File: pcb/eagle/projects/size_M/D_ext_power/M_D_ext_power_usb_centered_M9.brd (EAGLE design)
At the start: 33 parts, among them U1 LM66100DCKR

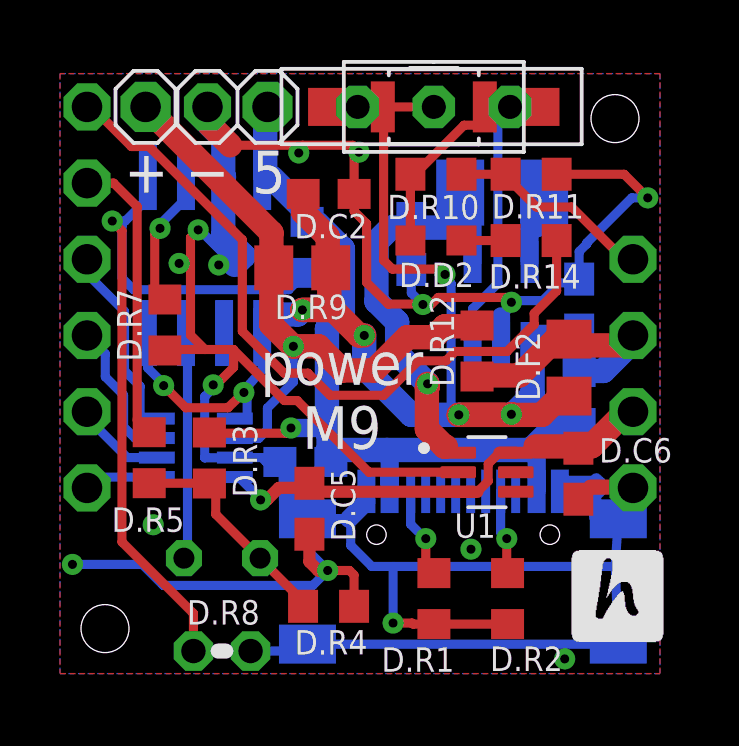
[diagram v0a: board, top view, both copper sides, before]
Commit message: turning on/off is performed by monitoring push button. D flip-flop is not necessary - has problem with button oscilations.
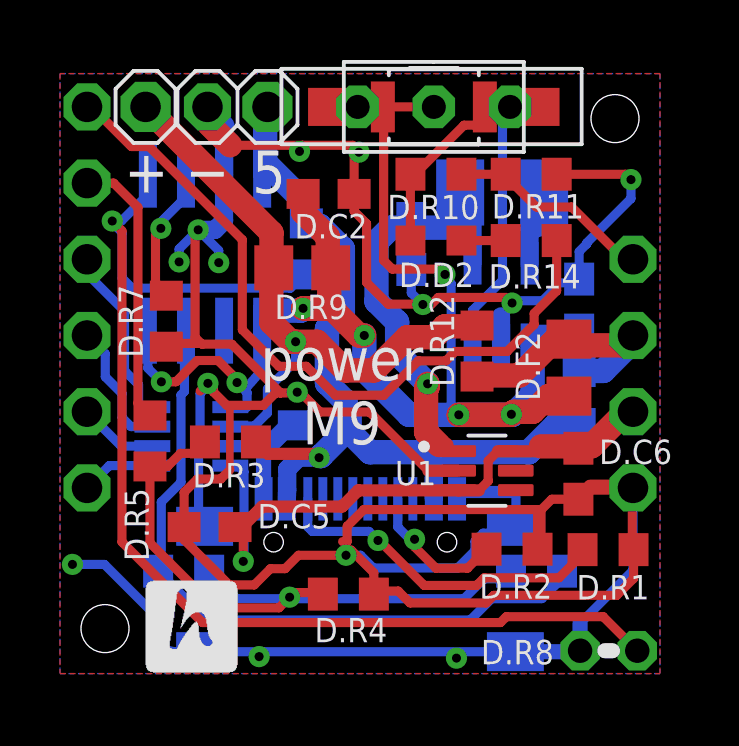
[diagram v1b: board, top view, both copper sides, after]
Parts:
- removed D.D1: LED_1.8, hugo:LED_1.8
- added LED1, LED2: (no value), led:CHIP-LED0603
- D.R10: value 150k -> 100k
- D.R11: value 330k -> 100k
- D.R14: value 680k -> 10k
- moved D.R8 12.9 mm to (18.8, 1.26), turned to 0 degrees
- moved D.R1 6.03 mm to (18.8, 4.63), turned to 0 degrees
- moved U$1 3.44 mm to (10.5, 2.50)
- moved D.C5 3.38 mm to (5.49, 5.38), turned to 0 degrees
- moved D.R2 1.65 mm to (15.6, 4.65), turned to 0 degrees
- moved D.C1 1.31 mm to (9.16, 8.77)
- moved D.R3 0.88 mm to (6.18, 8.22), turned to 0 degrees
- moved D.R4 0.78 mm to (10.1, 3.15)
- moved D.R5 0.56 mm to (3.50, 8.26)
- moved D.U3 0.41 mm to (4.88, 8.41)
- moved D.R7 0.14 mm to (4.05, 12.2)
- moved D.U1 0.08 mm to (5.33, 14.5)
- moved D.R6 0.06 mm to (8.71, 14.7)
- moved D.U2 0.05 mm to (15.2, 12.8)
- moved U1 0.05 mm to (14.7, 7.26)
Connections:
- net CHRG: now also LED1.A1, LED2.A1; no longer D.D1.2
- net N$3: now also LED1.C1, LED2.C1; no longer D.D1.1
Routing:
- net GND: track 123.5 -> 140.1 mm, vias 15 -> 14
- net N$3: track 7.58 -> 23.4 mm
- net CHRG: track 7.79 -> 22.5 mm, vias 0 -> 1
- net N$8: track 26.4 -> 40.4 mm
- net N$4: track 3.06 -> 11.5 mm
- net VCC: track 18.0 -> 22.4 mm
- net N$6: track 2.82 -> 4.88 mm
- net 5V: track 30.0 -> 31.7 mm
- net PA3: track 9.68 -> 9.13 mm

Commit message: power module finalizations (M9)
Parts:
- added D.R15: 0R, rcl:R0603
- moved U1 1.35 mm to (13.6, 6.50)
- moved D.R2 0.46 mm to (15.5, 4.19)
- moved D.U2 0.33 mm to (15.2, 12.5)
- moved D.D2 0.13 mm to (13.0, 15.1)
- moved D.C3 0.10 mm to (17.8, 12.7)
- moved D.R12 0.10 mm to (14.4, 11.4)
- moved D.R13 0.08 mm to (17.8, 9.63)
- moved D.R14 0.08 mm to (16.2, 15.0)
- moved D.F2 0.07 mm to (17.5, 10.7)
- moved D.R4 0.05 mm to (10.1, 3.20)
- moved D.R10 0.05 mm to (13.0, 17.2)
- moved D.R11 0.05 mm to (16.2, 17.2)
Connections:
- net VCC: now also D.R15.1
- net VCC1: now also D.R15.2
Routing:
- net GND: track 140.1 -> 131.9 mm, vias 14 -> 15
- net VCC: track 22.4 -> 23.6 mm
- net IN+: track 52.6 -> 53.3 mm

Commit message: PCB v9
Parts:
- removed D.C5: 100n, rcl:C0603
- removed D.R12, D.R13: 0, rcl:R0603
- removed D.R15: 0R, rcl:R0603
- removed D.R2: 5k1, rcl:R0603
- removed U1: LM66100DCKR, LM66100DCKR:SOT65P210X110-6N
- added Ḋ.C5: 100n, rcl:C0603
- added Ḋ.R12, Ḋ.R13: 0, rcl:R0603
- added Ḋ.R15: 0R, rcl:R0603
- added Ḋ.R2: 5k1, rcl:R0603
- added Ḋ.U3: LM66100DCKR, LM66100DCKR:SOT65P210X110-6N
- renumbered D.C1 to Ḋ.C1, D.C2 to Ḋ.C2, D.C3 to Ḋ.C3, D.C4 to Ḋ.C4, D.C6 to Ḋ.C6, D.D2 to Ḋ.D3, D.F2 to Ḋ.F2, D.J2 to Ḋ.J2, D.J3 to Ḋ.J3, D.L1 to Ḋ.L1, D.LIPOL to Ḋ.LIPOL, D.ON/OFF/RESET to Ḋ.BTN, D.R1 to Ḋ.R1, D.R10 to Ḋ.R10, D.R11 to Ḋ.R11, D.R14 to Ḋ.R14, D.R3 to Ḋ.R3, D.R4 to Ḋ.R4, D.R5 to Ḋ.R5, D.R6 to Ḋ.R6, D.R7 to Ḋ.R7, D.R8 to Ḋ.R8, D.R9 to Ḋ.R9, D.U1 to Ḋ.U1, D.U2 to Ḋ.U2, D.U3 to Ḋ.U4, LED1 to Ḋ.D1, LED2 to Ḋ.D2, U$1 to Ḋ.J1
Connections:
- net 5V: now also Ḋ.R13.1; no longer D.R13.1
- net GND: now also Ḋ.C5.1, Ḋ.R2.2, Ḋ.U3.2; no longer D.C5.1, D.R2.2, U1.2
- net IN-: now also Ḋ.R12.1; no longer D.R12.1
- net N$6: now also Ḋ.R2.1; no longer D.R2.1
- net VCC: now also Ḋ.C5.2, Ḋ.R15.1, Ḋ.U3.3, Ḋ.U3.6; no longer D.C5.2, D.R15.1, U1.3, U1.6
- net VCC1: now also Ḋ.R15.2, Ḋ.U3.1; no longer D.R15.2, U1.1
- net VOPT: now also Ḋ.R12.2, Ḋ.R13.2; no longer D.R12.2, D.R13.2
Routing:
- net N$6: track 4.64 -> 5.69 mm
- net GND: track 131.9 -> 132.7 mm
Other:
- board text added: "power M9c"
- board text removed: "power M9"
